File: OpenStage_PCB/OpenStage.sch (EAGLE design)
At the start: 73 parts, among them U2 ARDUINO_SHIELD

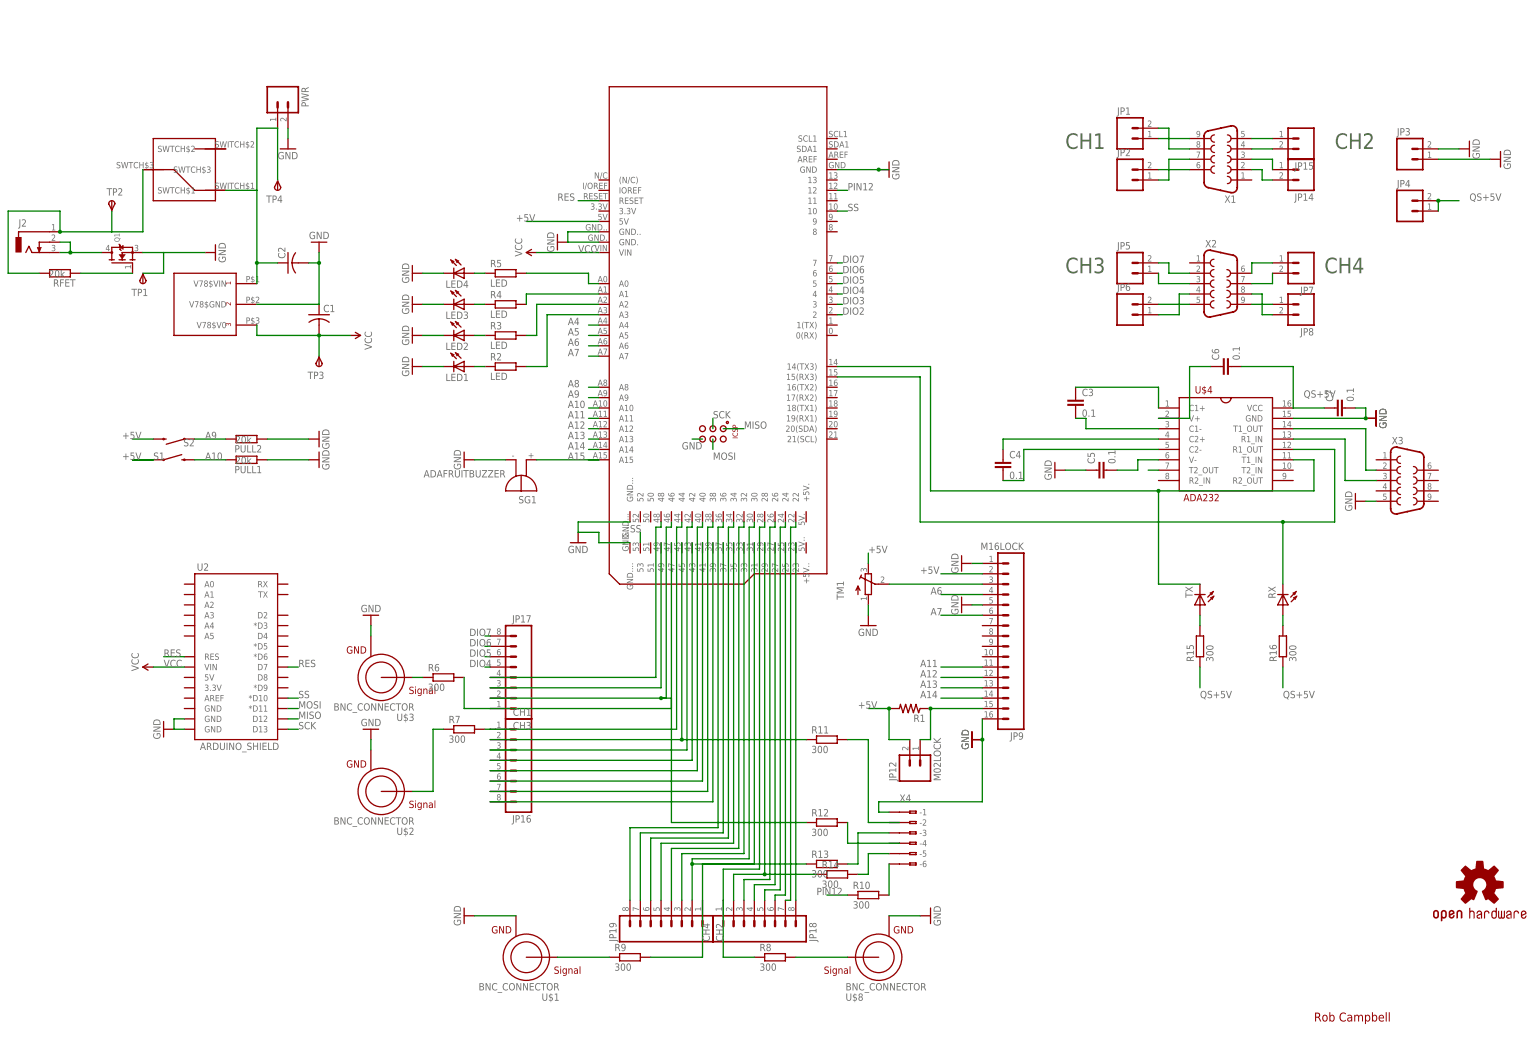
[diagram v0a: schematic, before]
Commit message: Replace quad-stepper board
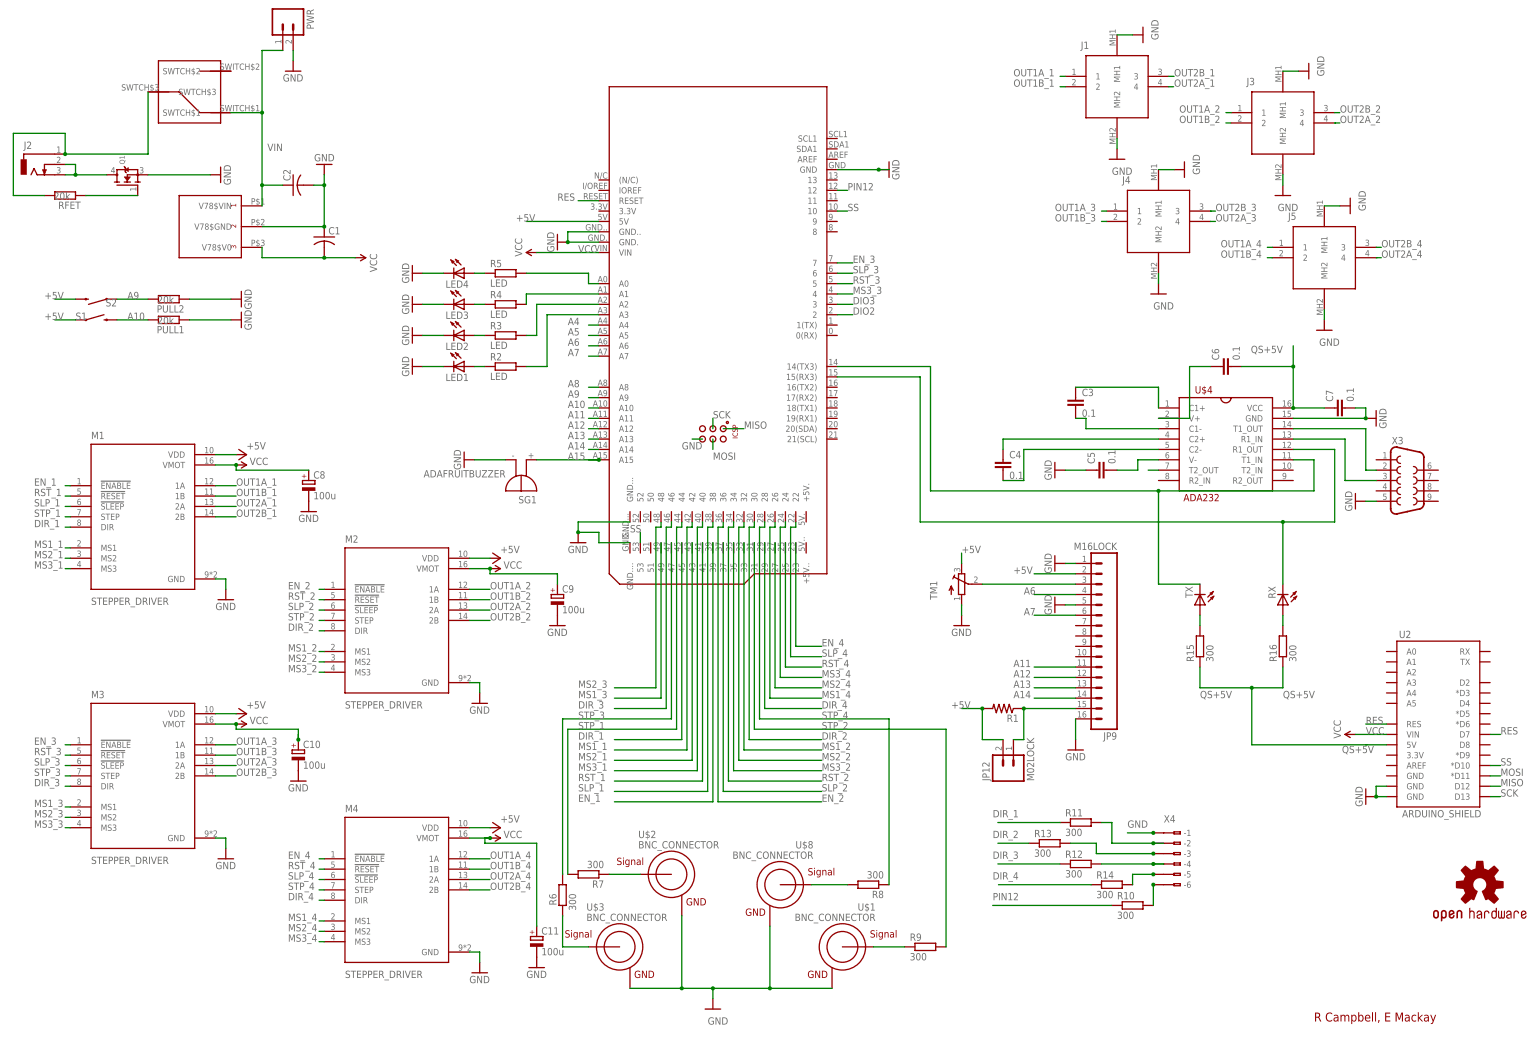
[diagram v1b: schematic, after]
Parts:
- removed JP1, JP14, JP15, JP2, JP5, JP6, JP7, JP8: (no value), SparkFun:M023.5MM_LOCK
- removed JP16: CH1, SparkFun:M08
- removed JP17: CH3, SparkFun:M08
- removed JP18: CH4, SparkFun:M08
- removed JP19: CH2, SparkFun:M08
- removed JP3, JP4: (no value), SparkFun:M02PTH
- removed TP1, TP2, TP3, TP4: TPSTP20SQ, testpad:TPSTP20SQ
- removed X1, X2: (no value), SparkFun-Connectors:DB9FEMALE
- added C10, C11, C8, C9: 100u, rcl:CPOL-EUE2.5-5
- added J1, J3, J4, J5: M8S-04PFFR-SF8001, SamacSys_Parts:M8S-04PFFR-SF8001
- added M1, M2, M3, M4: STEPPER_DRIVER, A4988_STEPPER_MOTOR_DRIVER_CARRIER:STEPPER_DRIVER
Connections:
- removed net DIO4: JP17.5, PCB2.4
- removed net DIO5: JP17.6, PCB2.5
- removed net DIO6: JP17.7, PCB2.6
- removed net DIO7: JP17.8, PCB2.7
- removed net N$11: JP19.2, PCB2.30, R13.1
- removed net N$12: JP19.3, PCB2.33
- removed net N$13: JP19.4, PCB2.32
- removed net N$14: JP19.5, PCB2.35
- removed net N$15: JP19.6, PCB2.34
- removed net N$16: JP19.7, PCB2.37
- removed net N$17: JP19.8, PCB2.36
- removed net N$18: JP16.7, PCB2.38
- removed net N$19: JP16.8, PCB2.39
- removed net N$2 (its old number): JP18.8, PCB2.23
- removed net N$20: JP16.6, PCB2.41
- removed net N$21: JP16.5, PCB2.40
- removed net N$22: JP16.4, PCB2.43
- removed net N$23: JP16.3, PCB2.42
- removed net N$24: JP16.2, PCB2.45, R11.1
- removed net N$25: JP16.1, PCB2.44, R7.2
- removed net N$26: JP17.1, PCB2.47, R6.2
- removed net N$27: JP17.2, PCB2.46, R12.1
- removed net N$28: JP17.3, PCB2.49
- removed net N$29: JP17.4, PCB2.48
- removed net N$3: JP18.7, PCB2.22
- removed net N$30: C2.1, PWR.1, TP4.PP, U$5.V78$VIN, U$6.SWTCH$1
- removed net N$32: JP19.1, PCB2.31, R9.2
- removed net N$4: JP18.6, PCB2.25
- removed net N$43: JP6.1, X2.4
- removed net N$45: JP6.2, X2.5
- removed net N$46: JP5.1, X2.3
- removed net N$47: JP5.2, X2.2
- removed net N$48: JP8.1, X2.9
- removed net N$49: JP8.2, X2.8
- removed net N$5: JP18.5, PCB2.24
- removed net N$50: JP7.2, X2.7
- removed net N$51: JP7.1, X2.6
- removed net N$52: JP15.1, X1.5
- removed net N$53: JP15.2, X1.4
- removed net N$54: JP14.1, X1.3
- removed net N$55: JP14.2, X1.2
- removed net N$56: JP1.2, X1.8
- removed net N$57: JP1.1, X1.9
- removed net N$58: JP2.2, X1.6
- removed net N$59: JP2.1, X1.7
- removed net N$6: JP18.4, PCB2.27
- removed net N$7: JP18.3, PCB2.26
- removed net N$8: JP18.2, PCB2.29, R14.1
- removed net N$9: JP18.1, PCB2.28, R8.1
- new net DIR_1: M1.DIR, PCB2.45, R11.1
- new net DIR_2: M2.DIR, PCB2.30, R13.1
- new net DIR_3: M3.DIR, PCB2.46, R12.1
- new net DIR_4: M4.DIR, PCB2.29, R14.1
- new net EN_1: M1.!ENABLE, PCB2.39
- new net EN_2: M2.!ENABLE, PCB2.36
- new net EN_3: M3.!ENABLE, PCB2.7
- new net EN_4: M4.!ENABLE, PCB2.23
- new net MS1_1: M1.MS1, PCB2.42
- new net MS1_2: M2.MS1, PCB2.33
- new net MS1_3: M3.MS1, PCB2.49
- new net MS1_4: M4.MS1, PCB2.26
- new net MS2_1: M1.MS2, PCB2.43
- new net MS2_2: M2.MS2, PCB2.32
- new net MS2_3: M3.MS2, PCB2.48
- new net MS2_4: M4.MS2, PCB2.27
- new net MS3_1: M1.MS3, PCB2.40
- new net MS3_2: M2.MS3, PCB2.35
- new net MS3_3: M3.MS3, PCB2.4
- new net MS3_4: M4.MS3, PCB2.24
- new net OUT1A_1: J1.1, M1.1A
- new net OUT1A_2: J3.1, M2.1A
- new net OUT1A_3: J4.1, M3.1A
- new net OUT1A_4: J5.1, M4.1A
- new net OUT1B_1: J1.2, M1.1B
- new net OUT1B_2: J3.2, M2.1B
- new net OUT1B_3: J4.2, M3.1B
- new net OUT1B_4: J5.2, M4.1B
- new net OUT2A_1: J1.4, M1.2A
- new net OUT2A_2: J3.4, M2.2A
- new net OUT2A_3: J4.4, M3.2A
- new net OUT2A_4: J5.4, M4.2A
- new net OUT2B_1: J1.3, M1.2B
- new net OUT2B_2: J3.3, M2.2B
- new net OUT2B_3: J4.3, M3.2B
- new net OUT2B_4: J5.3, M4.2B
- new net RST_1: M1.!RESET, PCB2.41
- new net RST_2: M2.!RESET, PCB2.34
- new net RST_3: M3.!RESET, PCB2.5
- new net RST_4: M4.!RESET, PCB2.25
- new net SLP_1: M1.!SLEEP, PCB2.38
- new net SLP_2: M2.!SLEEP, PCB2.37
- new net SLP_3: M3.!SLEEP, PCB2.6
- new net SLP_4: M4.!SLEEP, PCB2.22
- new net STP_1: M1.STEP, PCB2.44, R7.2
- new net STP_2: M2.STEP, PCB2.31, R9.2
- new net STP_3: M3.STEP, PCB2.47, R6.2
- new net STP_4: M4.STEP, PCB2.28, R8.1
- new net VIN: C2.1, PWR.1, U$5.V78$VIN, U$6.SWTCH$1
- net +5V: now also M1.VDD, M2.VDD, M3.VDD, M4.VDD
- net GND: now also C10.-, C11.-, C8.-, C9.-, J1.MH1, J1.MH2, J3.MH1, J3.MH2, J4.MH1, J4.MH2, J5.MH1, J5.MH2, M1.GND, M2.GND, M3.GND, M4.GND; no longer JP3.1, JP3.2, TP1.PP
- net N$73: no longer TP2.PP
- net N$77: now also X4.B-2
- net N$78: now also X4.B-4
- net QS+5V: now also U2.5V; no longer JP4.1, JP4.2
- net VCC: now also C10.+, C11.+, C8.+, C9.+, M1.VMOT, M2.VMOT, M3.VMOT, M4.VMOT; no longer TP3.PP
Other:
- note added: "R Campbell, E Mackay"
- note removed: "CH1"
- note removed: "CH2"
- note removed: "CH3"
- note removed: "CH4"
- note removed: "Rob Campbell"
- moved on the sheet: C1, C2, J2, JP12, JP9, PULL1, PULL2, PWR, Q1, R1, R10, R11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

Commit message: Generate gerbers for new PCB
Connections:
- removed net QS+5V: C6.2, C7.1, R15.1, R16.1, U$4.VCC, U2.5V
- new net N$3: U2.5V
- net +5V: now also C6.2, C7.1, R15.1, R16.1, U$4.VCC
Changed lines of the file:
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@@
 <part name="GND11" library="SparkFun-Aesthetics" deviceset="GND" device=""/>
 <part name="GND24" library="SparkFun-Aesthetics" deviceset="GND" device=""/>
+<part name="P+5" library="supply1" library_urn="urn:adsk.eagle:library:371" deviceset="+5V" device=""/>
 </parts>
 <sheets>
@@
 <instance part="GND24" gate="1" x="137.16" y="17.78" smashed="yes">
 <attribute name="VALUE" x="134.62" y="15.24" size="1.778" layer="96"/>
+</instance>
+<instance part="P+5" gate="1" x="327.66" y="115.57" smashed="yes">
+<attribute name="VALUE" x="326.39" y="115.57" size="1.778" layer="96" rot="R90"/>
 </instance>
 </instances>
@@
 <label x="132.08" y="200.66" size="1.778" layer="95"/>
 </segment>
+<segment>
+<pinref part="P+5" gate="1" pin="+5V"/>
+<pinref part="R15" gate="G$1" pin="1"/>
+<wire x1="299.72" y1="91.44" x2="299.72" y2="86.36" width="0.1524" layer="91"/>
+<label x="299.72" y="83.82" size="1.778" layer="95"/>
+<pinref part="R16" gate="G$1" pin="1"/>
+<wire x1="320.04" y1="91.44" x2="320.04" y2="86.36" width="0.1524" layer="91"/>
+<label x="320.04" y="83.82" size="1.778" layer="95"/>
+<wire x1="299.72" y1="86.36" x2="320.04" y2="86.36" width="0.1524" layer="91"/>
+<wire x1="320.04" y1="86.36" x2="327.66" y2="86.36" width="0.1524" layer="91"/>
+<junction x="320.04" y="86.36"/>
+<wire x1="327.66" y1="86.36" x2="327.66" y2="113.03" width="0.1524" layer="91"/>
+</segment>
+<segment>
+<pinref part="C7" gate="G$1" pin="1"/>
+<pinref part="U$4" gate="G$1" pin="VCC"/>
+<wire x1="322.58" y1="154.94" x2="330.2" y2="154.94" width="0.1524" layer="91"/>
+<junction x="322.58" y="154.94"/>
+<wire x1="322.58" y1="165.1" x2="322.58" y2="154.94" width="0.1524" layer="91"/>
+<pinref part="C6" gate="G$1" pin="2"/>
+<wire x1="309.88" y1="165.1" x2="322.58" y2="165.1" width="0.1524" layer="91"/>
+<label x="320.04" y="170.18" size="1.778" layer="95" rot="R180"/>
+<junction x="322.58" y="165.1"/>
+<wire x1="322.58" y1="165.1" x2="322.58" y2="170.18" width="0.1524" layer="91"/>
+</segment>
 </net>
 <net name="A15" class="0">
@@
 </segment>
 </net>
-<net name="QS+5V" class="0">
-<segment>
-<pinref part="R15" gate="G$1" pin="1"/>
-<wire x1="299.72" y1="91.44" x2="299.72" y2="86.36" width="0.1524" layer="91"/>
-<label x="299.72" y="83.82" size="1.778" layer="95"/>
-<pinref part="R16" gate="G$1" pin="1"/>
-<wire x1="320.04" y1="91.44" x2="320.04" y2="86.36" width="0.1524" layer="91"/>
-<label x="320.04" y="83.82" size="1.778" layer="95"/>
-<wire x1="299.72" y1="86.36" x2="312.42" y2="86.36" width="0.1524" layer="91"/>
-<pinref part="U2" gate="G$1" pin="5V"/>
-<wire x1="312.42" y1="86.36" x2="320.04" y2="86.36" width="0.1524" layer="91"/>
-<wire x1="345.44" y1="72.39" x2="340.614" y2="72.39" width="0.1524" layer="91"/>
-<label x="334.518" y="70.358" size="1.778" layer="95"/>
-<wire x1="340.614" y1="72.39" x2="340.36" y2="72.39" width="0.1524" layer="91"/>
-<wire x1="312.42" y1="86.36" x2="312.42" y2="72.39" width="0.1524" layer="91"/>
-<wire x1="312.42" y1="72.39" x2="340.36" y2="72.39" width="0.1524" layer="91"/>
-<junction x="312.42" y="86.36"/>
-</segment>
-<segment>
-<pinref part="C7" gate="G$1" pin="1"/>
-<pinref part="U$4" gate="G$1" pin="VCC"/>
-<wire x1="322.58" y1="154.94" x2="330.2" y2="154.94" width="0.1524" layer="91"/>
-<junction x="322.58" y="154.94"/>
-<wire x1="322.58" y1="165.1" x2="322.58" y2="154.94" width="0.1524" layer="91"/>
-<pinref part="C6" gate="G$1" pin="2"/>
-<wire x1="309.88" y1="165.1" x2="322.58" y2="165.1" width="0.1524" layer="91"/>
-<label x="320.04" y="170.18" size="1.778" layer="95" rot="R180"/>
-<junction x="322.58" y="165.1"/>
-<wire x1="322.58" y1="165.1" x2="322.58" y2="170.18" width="0.1524" layer="91"/>
-</segment>
-</net>
 <net name="A14" class="0">
 <segment>
@@
 </segment>
 </net>
+<net name="N$3" class="0">
+<segment>
+<pinref part="U2" gate="G$1" pin="5V"/>
+<wire x1="345.44" y1="72.39" x2="340.36" y2="72.39" width="0.1524" layer="91"/>
+<label x="334.518" y="70.358" size="1.778" layer="95"/>
+</segment>
+</net>
